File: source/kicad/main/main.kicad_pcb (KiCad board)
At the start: 2 copper layers, 19 parts

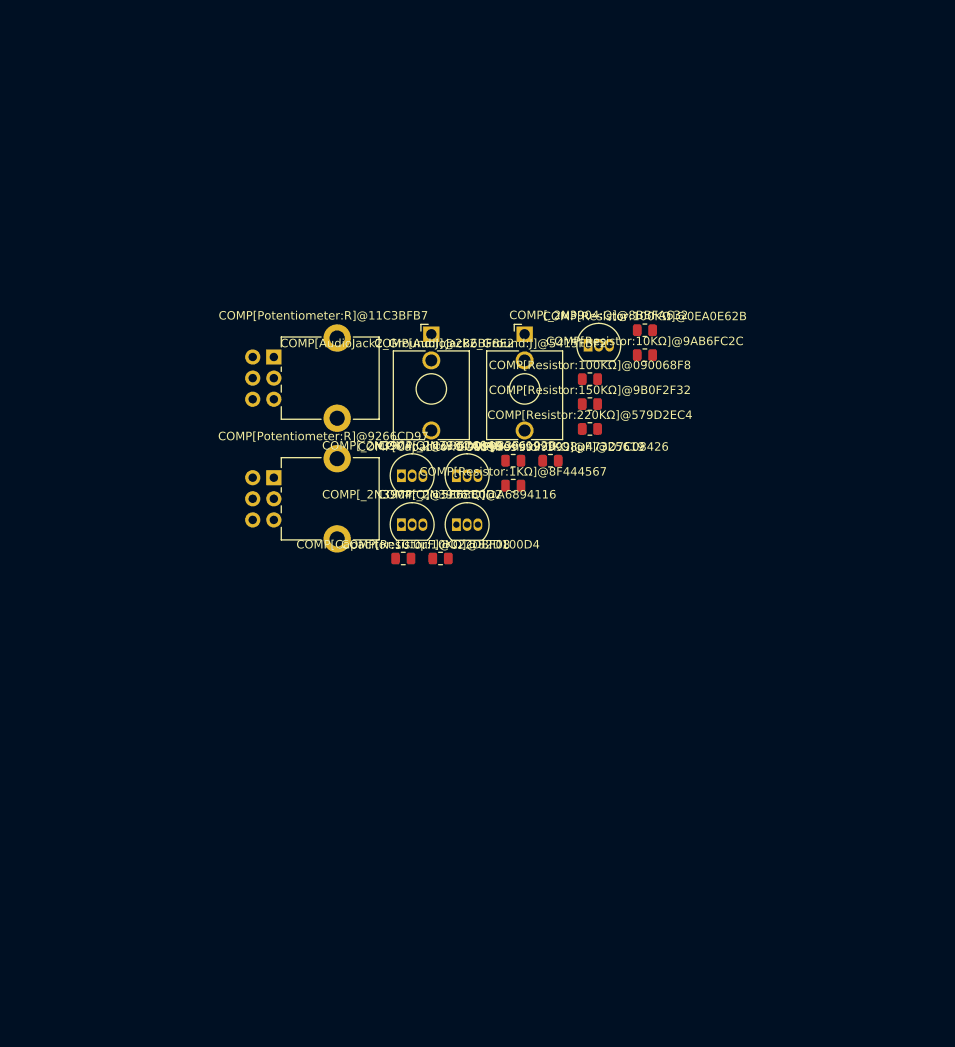
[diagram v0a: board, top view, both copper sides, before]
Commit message: Prepare for new faebryk release
- fix wrong connections
- fix wrong resistor values
- add missing pot
- remove add_all function from local lib
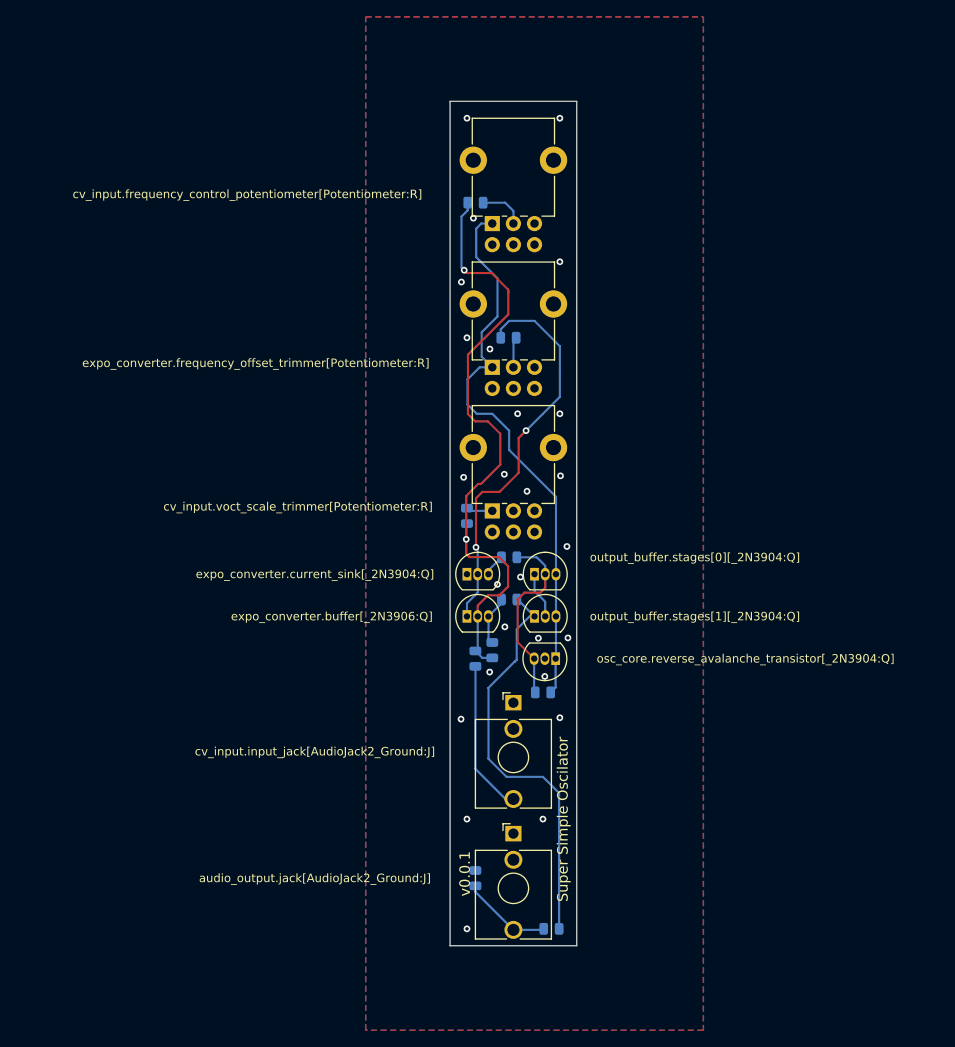
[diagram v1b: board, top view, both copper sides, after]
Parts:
- removed COMP[AudioJack2_Ground:J]@2B6BF8E2, COMP[AudioJack2_Ground:J]@5415FBF2: J, Connector_Audio:Jack_3.5mm_QingPu_WQP-PJ398SM_Vertical_CircularHoles
- removed COMP[Capacitor:10.0µF]@022D8F08: 10.0µF, Resistor_SMD:R_0805_2012Metric
- removed COMP[Capacitor:9.999999999999998µF]@D7C08426: 9.999999999999998µF, Resistor_SMD:R_0805_2012Metric
- removed COMP[Potentiometer:R]@11C3BFB7, COMP[Potentiometer:R]@9266CD97: R, Potentiometer_THT:Potentiometer_Alpha_RD902F-40-00D_Dual_Vertical_CircularHoles
- removed COMP[Resistor:100KΩ]@090068F8, COMP[Resistor:100KΩ]@0EA0E62B: 100KΩ, Resistor_SMD:R_0805_2012Metric
- removed COMP[Resistor:10KΩ]@82D100D4, COMP[Resistor:10KΩ]@9AB6FC2C: 10KΩ, Resistor_SMD:R_0805_2012Metric
- removed COMP[Resistor:150KΩ]@9B0F2F32: 150KΩ, Resistor_SMD:R_0805_2012Metric
- removed COMP[Resistor:1KΩ]@47325619, COMP[Resistor:1KΩ]@8F444567: 1KΩ, Resistor_SMD:R_0805_2012Metric
- removed COMP[Resistor:220KΩ]@579D2EC4: 220KΩ, Resistor_SMD:R_0805_2012Metric
- removed COMP[_2N3904:Q]@0D57484B, COMP[_2N3904:Q]@33F6192B, COMP[_2N3904:Q]@5E68B0D2, COMP[_2N3904:Q]@8BBFA632, COMP[_2N3906:Q]@A6894116: Q, Package_TO_SOT_THT:TO-92_Inline
- added G***: LOGO, logo:faebryk_logo, B.Cu at (137.5, 57.1)
- added audio_output.ac_coupling_capacitor[Capacitor:9.999999999999998µF]: 9.999999999999998µF, Resistor_SMD:R_0805_2012Metric, B.Cu at (142.0, 148.0)
- added audio_output.jack[AudioJack2_Ground:J]: J, Connector_Audio:Jack_3.5mm_QingPu_WQP-PJ398SM_Vertical_CircularHoles, F.Cu at (137.5, 136.7)
- added audio_output.pull_down_resistor[Resistor:10KΩ]: 10KΩ, Resistor_SMD:R_0805_2012Metric, B.Cu at (133.0, 142.0)
- added cv_input.freq_devider_mix_resistor[Resistor:150KΩ]: 150KΩ, Resistor_SMD:R_0805_2012Metric, B.Cu at (133.0, 62.0)
- added cv_input.frequency_control_potentiometer[Potentiometer:R]: R, Potentiometer_THT:Potentiometer_Alpha_RD902F-40-00D_Dual_Vertical_CircularHoles, F.Cu at (135.0, 64.5)
- added cv_input.input_impendace_resistor[Resistor:100KΩ]: 100KΩ, Resistor_SMD:R_0805_2012Metric, B.Cu at (133.0, 116.0)
- added cv_input.input_jack[AudioJack2_Ground:J]: J, Connector_Audio:Jack_3.5mm_QingPu_WQP-PJ398SM_Vertical_CircularHoles, F.Cu at (137.5, 121.2)
- added cv_input.negative_bias_resistor[Resistor:220KΩ]: 220KΩ, Resistor_SMD:R_0805_2012Metric, B.Cu at (135.0, 115.0)
- added cv_input.voct_min_resistor[Resistor:1.0KΩ]: 1.0KΩ, Resistor_SMD:R_0805_2012Metric, B.Cu at (132.0, 99.1)
- added cv_input.voct_scale_trimmer[Potentiometer:R]: R, Potentiometer_THT:Potentiometer_Alpha_RD902F-40-00D_Dual_Vertical_CircularHoles, F.Cu at (135.0, 98.5)
- added expo_converter.buffer[_2N3906:Q]: Q, Package_TO_SOT_THT:TO-92_Inline, F.Cu at (132.0, 111.0)
- added expo_converter.current_sink[_2N3904:Q]: Q, Package_TO_SOT_THT:TO-92_Inline, F.Cu at (132.0, 106.0)
- added expo_converter.frequency_offset_current_min_resistor[Resistor:100KΩ]: 100KΩ, Resistor_SMD:R_0805_2012Metric, B.Cu at (136.9, 78.0)
- added expo_converter.frequency_offset_trimmer[Potentiometer:R]: R, Potentiometer_THT:Potentiometer_Alpha_RD902F-40-00D_Dual_Vertical_CircularHoles, F.Cu at (135.0, 81.5)
- added osc_core.charge_capacitor[Capacitor:10.0µF]: 10.0µF, Resistor_SMD:R_0805_2012Metric, B.Cu at (141.0, 120.0)
- added osc_core.current_limiting_resistor[Resistor:1KΩ]: 1KΩ, Resistor_SMD:R_0805_2012Metric, B.Cu at (137.0, 104.0)
- added osc_core.reverse_avalanche_transistor[_2N3904:Q]: Q, Package_TO_SOT_THT:TO-92_Inline, F.Cu at (142.5, 116.0)
- added output_buffer.current_limiting_resistor[Resistor:10KΩ]: 10KΩ, Resistor_SMD:R_0805_2012Metric, B.Cu at (137.0, 109.0)
- added output_buffer.stages[0][_2N3904:Q]: Q, Package_TO_SOT_THT:TO-92_Inline, F.Cu at (140.0, 106.0)
- added output_buffer.stages[1][_2N3904:Q]: Q, Package_TO_SOT_THT:TO-92_Inline, F.Cu at (140.0, 111.0)
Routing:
- net cv_input[cv_input:virt]-expo_converter[expo_converter:virt]: track 0.00 -> 74.4 mm, vias 0 -> 2
- net cv_input.frequency_control_potentiometer.resistors[0][Resistor:virt]-output_buffer[output_buffer:virt]-osc_core[osc_core:virt]:2-expo_converter.frequency_offset_trimmer.resistors[0][Resistor:virt]-[Kassutronics_Avalance_VCO:virt]:2-cv_input[cv_input:virt]:3-expo_converter[expo_converter:virt]:4: track 0.00 -> 67.2 mm
- net audio_output[audio_output:virt]:2-output_buffer[output_buffer:virt]:3: track 0.00 -> 48.5 mm
- net expo_converter.frequency_offset_current_min_resistor[Resistor:100KΩ]-expo_converter.buffer[_2N3906:Q]-expo_converter.current_sink[_2N3904:Q]: track 0.00 -> 47.6 mm, vias 0 -> 2
- net osc_core[osc_core:virt]:3-output_buffer[output_buffer:virt]:4: track 0.00 -> 22.1 mm
- net cv_input.input_jack[AudioJack2_Ground:J]-cv_input.input_impendace_resistor[Resistor:100KΩ]: track 0.00 -> 18.1 mm
- net audio_output.ac_coupling_capacitor[Capacitor:9.999999999999998µF]-audio_output.jack[AudioJack2_Ground:J]-audio_output.pull_down_resistor[Resistor:10KΩ]: track 0.00 -> 10.7 mm
- net [Kassutronics_Avalance_VCO:virt]:3-cv_input[cv_input:virt]:4-expo_converter[expo_converter:virt]:5-output_buffer[output_buffer:virt]:2: track 0.00 -> 5.92 mm
- net output_buffer.stages[1][_2N3904:Q]-output_buffer.stages[0][_2N3904:Q]: track 0.00 -> 5.53 mm
- net cv_input.frequency_control_potentiometer.resistors[0][Resistor:virt]:2-cv_input.frequency_control_potentiometer.resistors[1][Resistor:virt]:2: track 0.00 -> 5.49 mm
- net expo_converter.frequency_offset_trimmer.resistors[0][Resistor:virt]:2-expo_converter.frequency_offset_trimmer.resistors[1][Resistor:virt]:2: track 0.00 -> 3.63 mm
- net cv_input.voct_scale_trimmer.resistors[0][Resistor:virt]: track 0.00 -> 3.13 mm
- net osc_core[osc_core:virt]-expo_converter[expo_converter:virt]:2: track 0.00 -> 2.64 mm
- net [Kassutronics_Avalance_VCO:virt]-cv_input[cv_input:virt]:2-cv_input.voct_scale_trimmer.resistors[0][Resistor:virt]:2-expo_converter[expo_converter:virt]:3-expo_converter.frequency_offset_trimmer.resistors[1][Resistor:virt]-cv_input.frequency_control_potentiometer.resistors[1][Resistor:virt]-cv_input.voct_scale_trimmer.resistors[1][Resistor:virt]:2-audio_output[audio_output:virt]: vias 0 -> 26
- added copper zone on B.Cu, net [Kassutronics_Avalance_VCO:virt]-cv_input[cv_input:virt]:2-cv_input.voct_scale_trimmer.resistors[0][Resistor:virt]:2-expo_converter[expo_converter:virt]:3-expo_converter.frequency_offset_trimmer.resistors[1][Resistor:virt]-cv_input.frequency_control_potentiometer.resistors[1][Resistor:virt]-cv_input.voct_scale_trimmer.resistors[1][Resistor:virt]:2-audio_output[audio_output:virt]
- added copper zone on F.Cu, net [Kassutronics_Avalance_VCO:virt]-cv_input[cv_input:virt]:2-cv_input.voct_scale_trimmer.resistors[0][Resistor:virt]:2-expo_converter[expo_converter:virt]:3-expo_converter.frequency_offset_trimmer.resistors[1][Resistor:virt]-cv_input.frequency_control_potentiometer.resistors[1][Resistor:virt]-cv_input.voct_scale_trimmer.resistors[1][Resistor:virt]:2-audio_output[audio_output:virt]
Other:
- board outline added: 15 x 100 mm
- board text added: "Super Simple Oscilator"
- board text added: "v0.0.1"
